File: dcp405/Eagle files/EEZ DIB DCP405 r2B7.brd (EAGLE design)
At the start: 180 x 95 mm, 308 parts, among them IC1 LTC3864EMSE#PBF, IC10 MC33272ADR2G, IC11 LTC2050HVCS8#PBF, IC12 74AUP1G74DC.125, IC13 MCP23S17-E/SS, IC14 REF5025AIDR, IC15 TC77-5.0MCTTR, IC16 DAC8552IDGKR, IC17 SN74LVC1G3157DCKR, IC18 ADS1120IPWR, IC19 LM293D, IC2 TPS54060DGQ, IC20 MAX9141ESA, IC3 SI8641BB-B-IS1, IC4 SN74LVC1G139DCUR, IC5 MC78L05, IC6 MC79L05, IC7 SI8641BB-B-IS1, IC8 M24C32-WMN6P, IC9 MC33272ADR2G, J1 4907, J2 FCR7350R, J3 FCR7350B, K1 G6K-2F-5DC, Q1 SUD19P06-60, Q10 PSMN0R9-25YLC, Q11 PSMN0R9-25YLC, Q12 BSS84P, Q13 BTA26-600, Q14 FMMT493TA, Q15 2N7002, Q16 2N7002, Q17 2N7002, Q18 MMBT5401, Q19 MMBT5551, Q2 MMBT5401, Q20 MMBT5551, Q21 2N7002, Q3 D45H11FP, Q4 D45H11FP, Q5 FQPF11P06 or FQPF27P06, Q6 BCP56-16.115, Q7 MMBT5401, Q8 NZT605, Q9 BSS205NH6327XTSA1, X1 39-30-1020, X2 77317-104-28LF, X3 1844249, X4 DS1024-2*10R0

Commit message: #49
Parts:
- added C97: 10n, rcl:C0805
- added R107: 470R, rcl:R0805
- added R108: 100K, rcl:R0805
- C41: value 1n -> 220p
- C42, C57, C58: value 33p -> 100n; device rcl:C0805 -> rcl:C0603
- C43, C60: value 330p -> 33p
- C44: value 1n -> 330p
- C46: value 10n -> 220p
- C48: value 100n -> 10n; device rcl:C0603 -> rcl:C0805
- C50, C67, C78, C80: value 1u -> 100n; device rcl:C0805 -> rcl:C0603
- C51, C72, C88: value 10n -> 100n; device rcl:C0805 -> rcl:C0603
- C52: value 6n8 -> 1u
- C53: value 1u -> 10n
- C54: value 100n -> 6n8; device rcl:C0603 -> rcl:C0805
- C55, C69, C70, C79, C81: value 100n -> 1u; device rcl:C0603 -> rcl:C0805
- C59: value 4n7 -> 33p
- C61: value 1n -> 4n7
- C62: value 100n -> 330p; device rcl:C0603 -> rcl:C0805
- C63, C86: value 100n -> 1n; device rcl:C0603 -> rcl:C0805
- C64: value 4u7 -> 100n; device rcl:C1206 -> rcl:C0603
- C66: value 4u7 tant. -> 4u7; device EEZ_Lib1:EC1206 -> rcl:C1206
- C68: value 1u -> 4u7 tant.; device rcl:C0805 -> EEZ_Lib1:EC1206
- C73: value 4n7 -> 100n; device rcl:C0805 -> rcl:C0603
- C77: value 100n -> 4n7; device rcl:C0603 -> rcl:C0805
- C82: value N.C. -> 100n; device rcl:C0805 -> rcl:C0603
- C83: value 100n -> N.C.; device rcl:C0603 -> rcl:C0805
- C84: value 1n -> 100n; device rcl:C0805 -> rcl:C0603
- C89: value 470n -> 10n; device rcl:C1206 -> rcl:C0805
- C90: value HHXC630A330MHA0G -> 470n; device EEZ_Lib1:CAPAE830X1050N -> rcl:C1206
- C91: value 10n/200V -> HHXC630A330MHA0G; device rcl:C1206 -> EEZ_Lib1:CAPAE830X1050N
- C92: value N.C. -> 10n/200V; device EEZ_Lib1:ECAP2/5 -> rcl:C1206
- C93: device rcl:C0805 -> EEZ_Lib1:ECAP2/5
- C95: value 10n/200V -> N.C.; device rcl:C1206 -> rcl:C0805
- C96: value 10n -> 10n/200V; device rcl:C0805 -> rcl:C1206
- R100, R46: value 10K -> 2K2
- R101: value 1R -> 10K
- R102: value 750R -> 10K
- R103: value 47K -> 1R
- R104: value 330R -> 750R
- R105: value 470R -> 47K
- R106: value 100K -> 330R
- R50: value 4K7 -> 10K
- R51, R67: value 100K -> 4K7
- R52: value 39K 0.1% -> 100K
- R53: value 820R 0.1% -> 2K2
- R54: value 47K -> 2K2
- R55: value 2K2 -> 39K 0.1%
- R56: value 1R -> 820R 0.1%; device rcl:R1206 -> rcl:R0805
- R57, R62: value 10K -> 47K
- R58: value 1K -> 1R; device rcl:R0805 -> rcl:R1206
- R59: value 39K 0.1% -> 10K
- R60: value 47K -> 1K
- R61: value 0R010 (low TCR) -> 39K 0.1%; device EEZ_Lib1:R_2512-4WIRE -> rcl:R0805
- R63: value 820R 0.1% -> 0R010 (low TCR); device rcl:R0805 -> EEZ_Lib1:R_2512-4WIRE
- R64, R85: value 1K -> 10K
- R65: value 4K7 -> 820R 0.1%
- R66, R99: value 10K -> 1K
- R68: value 270R -> 10K
- R69: value 2K2 -> 100K
- R70: value 470R -> 270R
- R71, R74: value 470R -> 2K2
- R72, R73, R76: value 2K2 -> 470R
- R77: value 10R -> 2K2; device rcl:R1206 -> rcl:R0805
- R78: value 330R -> 2K2
- R79: value 4K7 -> 10R; device rcl:R0805 -> rcl:R1206
- R80: value 470R -> 330R
- R81: value 10K -> 4K7
- R82: value 4K7 -> 470R
- R84: value 330R -> 4K7
- R87: value AC01000002207JA100 -> 1K; device rcl:0411/15 -> rcl:R0805
- R88: value 10K -> 330R
- R89: value 10K -> AC01000002207JA100; device rcl:R0805 -> rcl:0411/15
- R90: value 100K -> 10K
- R91: value 6R2 -> 10K
- R92: value 4K7 -> 100K
- R93: value 10K -> 6R2
- R95: value 330R -> 10K
- R96: value 750R -> 4K7
- R97: value 1K -> 330R
- R98: value 2K2 -> 750R
- moved R74 110.9 mm to (110.7, 24.7), turned to 0 degrees
- moved R72 108.6 mm to (11.8, 69.5), turned to 270 degrees
- moved R68 108.5 mm to (116.2, 63.4)
- moved R84 108.0 mm to (117.7, 53.8), turned to 90 degrees
- moved R76 107.5 mm to (12.4, 76.0), turned to 180 degrees
- moved R73 105.6 mm to (11.8, 65.6), turned to 270 degrees
- moved R96 100.9 mm to (117.7, 49.8), turned to 270 degrees
- moved C88 90.5 mm to (115.7, 45.4), turned to 90 degrees
- moved R95 86.5 mm to (113.9, 56.1)
- moved C72 85.5 mm to (92.3, 30.0)
- moved R89 78.4 mm to (33.3, 61.7)
- moved R69 73.9 mm to (125.5, 65.6), turned to 0 degrees
- moved R82 72.3 mm to (45.5, 49.7), turned to 270 degrees
- moved R88 67.5 mm to (12.4, 79.9), turned to 180 degrees
- moved R93 66.3 mm to (48.4, 45.8)
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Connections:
- new net N$10: C47.1, R53.1, R54.2
- new net N$24: C42.1, R45.1, R46.2
- net !DP_DRIVE: now also R71.1; no longer R69.1
- net !IOEXP_RST: now also C62.1, R66.2; no longer C60.1, R64.2
- net !OVP_FAULT: now also C63.1, R67.2; no longer C61.1, R65.2
- net !SET_DP: now also R69.2; no longer R67.2
- net +5V: now also C63.2, C64.2, C67.1, C79.2, R101.2, R68.1, R69.1, R81.2, R94.2; no longer C60.2, C61.2, C63.1, C77.2, R64.1, R65.1, R79.2, R92.2, R99.2
- net +VREF: now also C68.+, C72.2, C82.2; no longer C66.+, C70.2, C81.2
- net 50MA_S: now also R58.1; no longer R53.1
- net 5A_S: now also R63.2; no longer R61.2
- net AUX_IN: now also R72.1; no longer C72.2, R70.1
- net CC_ACTIVE: now also R94.1, R96.2; no longer R92.1, R94.2
- net CC_LED: now also R88.2; no longer R86.2
- net CURR_50MA: now also R57.2; no longer R54.2
- net CURR_5A: now also R62.2; no longer R60.2
- net CV_ACTIVE: now also R81.1, R84.2; no longer R79.1, R82.2
- net CV_LED: now also R86.1; no longer R84.1
- net D_CC: now also R88.1; no longer R86.1
- net D_CV: now also R86.2; no longer R84.2
- net GCOM: now also R55.1; no longer R52.1
- net GND: now also C42.2, C49.2, C52.1, C56.2, C57.1, C58.1, C64.1, C66.2, C68.-, C69.2, C70.2, C71.1, C73.2, C75.1, C76.2, C82.1, C83.2, C88.1, R105.1, R108.1, R52.1, R57.1, R62.1, R70.2, R76.1, R85.2, R92.1, R93.1; no longer C46.1, C49.1, C54.2, C56.1, C62.1, C63.2, C64.2, C66.-, C68.2, C69.1, C70.1, C71.2, C73.1, C75.2, C76.1, C82.2, C83.1, R103.1, R106.1, R51.1, R54.1, R60.1, R68.2, R74.1, R83.2, R90.1, R91.1
- net ISENSE+: now also R55.2, R56.2; no longer R52.2, R53.2
- net ISENSE-: now also C60.1, R61.1, R65.2; no longer C58.1, R59.1, R63.2
- net I_MON: now also C60.2, R59.1, R61.2, R78.1; no longer C58.2, R57.1, R59.2, R76.1
- net I_SERVO: now also C54.2, C59.2, R95.1; no longer C52.2, C57.2, R93.1
- net I_SET: now also R54.1, R74.1; no longer R55.1, R72.1
- net LOOP_CTRL: now also R91.2; no longer R89.2
- net N$105: now also R84.1; no longer R82.1
- net N$106: now also R96.1; no longer R94.1
- net N$107: now also C89.2, R100.2, R97.1; no longer C88.2, R95.1, R96.2
- net N$108: now also R102.2; no longer R100.2
- net N$109: now also R99.1; no longer R97.1
- net N$11: now also R58.2, R63.2S; no longer R56.2, R61.2S
- net N$110: now also C97.1, R104.1, R106.2; no longer C96.1, R102.1, R104.2
- net N$112: now also R102.1, R105.2; no longer R100.1, R103.2
- net N$113: now also C90.2, R103.2; no longer C89.2, R101.2
- net N$114: now also R107.1; no longer R105.1
- net N$12: now also R70.1; no longer R68.1
- net N$120: now also R107.2; no longer R105.2
- net N$121: now also R76.2; no longer R74.2
- net N$13: now also R87.2; no longer R85.2
- net N$14: now also C44.1; no longer C43.1
- net N$15: now also R89.2; no longer R87.2
- net N$153: now also R83.2; no longer R81.2
- net N$158: now also C43.1; no longer C42.1
- net N$161: now also R95.2; no longer R93.2
- net N$17: now also R72.2, R73.1; no longer R70.2, R71.1
- net N$170: now also R91.1; no longer R89.1
- net N$173: now also R100.1, R99.2; no longer R97.2, R98.1
- net N$18: now also R82.1; no longer R80.1
- net N$19: now also R93.2; no longer R91.2
- net N$200: now also R63.1S, R65.1; no longer R61.1S, R63.1
- net N$21: now also R87.1, R92.2; no longer R85.1, R90.2
- net N$31: now also C86.2, R90.2; no longer C85.2, R88.2
- net N$32: now also R73.2; no longer R71.2
- net N$33: now also C85.2, R80.2, R85.1; no longer C84.2, R78.2, R83.1
- net N$37: now also C54.1, R60.1; no longer C52.1, R58.1
- net N$42: now also R71.2; no longer R69.2
- net N$56: now also R68.2; no longer R66.2
- net N$70: now also C81.2, R79.2; no longer C79.2, R77.2
- net N$71: now also C70.1; no longer C68.1
- net N$72: now also C74.2, R74.2; no longer C73.2, R72.2
- net N$73: now also C77.2, R77.2; no longer C76.2, R75.2
- net N$80: now also C75.2, R75.2; no longer C74.2, R73.2
- net N$81: now also C76.1, R78.2; no longer C75.1, R76.2
- net N$82: now also R53.2; no longer R55.2
- net N$84: now also R51.2; no longer R46.2
- net N$88: now also C61.2, R64.1; no longer C59.2, R62.1
- net N$89: now also C59.1, R59.2, R60.2, R64.2; no longer C57.1, R57.2, R58.2, R62.2
- net N$91: now also C46.2, R51.1; no longer C44.2, R50.1
- net OUTC+: now also C92.1, C93.+, C95.1; no longer C91.1, C92.+, C93.1
- net OUTC-: now also C93.-, C96.2; no longer C92.-, C93.2
- net OUTF+: now also R82.2; no longer R80.2
- net PE: now also C92.2, C96.1; no longer C91.2, C95.1
- net POST_OE: now also R52.2; no longer R51.2
- net POST_OUT+: now also C46.1, C61.1; no longer C44.1, C59.1
- net POST_OUT-: now also C91.-, C97.2, R103.1, R106.1; no longer C90.-, C96.2, R101.1, R104.1
- net POST_OUTF+: now also C90.1, C91.+, R97.2; no longer C88.1, C90.+, R95.2
- net PREG_OUT-: now also R63.1, R89.1; no longer R61.1, R87.1
- net RSENSE: now also R108.2; no longer R106.2
- net SENSE+: now also R98.1; no longer R96.1
- net SENSE-: now also R104.2; no longer R102.2
- net SENSE_ERR: now also R101.1; no longer R99.1
- net U_MON: now also C43.2, R50.1, R77.1, R80.1; no longer C42.2, R46.1, R75.1, R78.1
- net U_SERVO: now also C44.2, R83.1; no longer C43.2, R81.1
- net U_SET: now also R75.1, R90.1; no longer R73.1, R88.1
- net U_SET_OUT: now also R46.1; no longer R45.1
- net V+: now also C49.1, C51.2, C52.2, C66.1, C69.1, C71.2, C73.1, C83.1, C84.2, C87.2, R79.1; no longer C46.2, C47.1, C49.2, C64.1, C67.1, C69.2, C71.1, C82.1, C83.2, C86.2, R77.1
- net V-: now also C56.1, C57.2, C58.2, C88.2; no longer C51.2, C54.1, C56.2, C87.2
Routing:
- net U_SET: track 67.1 -> 61.6 mm, vias 2 -> 4
- net N$10: track 0.00 -> 3.78 mm
- net N$24: track 0.00 -> 3.69 mm
- net AUX_IN: track 104.5 -> 101.4 mm
- net GND: track 195.9 -> 198.4 mm
- net I_SET: track 28.4 -> 26.2 mm
- net U_SET_OUT: track 7.11 -> 5.30 mm, vias 2 -> 0
- net AUX_USET_SW: track 168.9 -> 167.2 mm
- net POST_OUT-: track 234.3 -> 233.3 mm
- net SENSE-: track 74.1 -> 73.0 mm
- net SENSE+: track 75.5 -> 74.5 mm
- net +VREF: track 59.2 -> 60.3 mm
- net U_MON: track 75.9 -> 76.6 mm
- net V-: track 129.9 -> 130.4 mm
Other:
- board text added: "B"
- board text added: "EEZ DIB DCP405 (10/2019 r2B7)"
- board text added: "EEZ DIB DCP405 (10/2019 r2B7) DC power source 0-40V / 5A Project source code: github.com/eez-open"
- board text removed: "EEZ DIB DCP405 (09/2019 r2B6)"
- board text removed: "EEZ DIB DCP405 (09/2019 r2B6) DC power source 0-40V / 5A Project source code: github.com/eez-open"

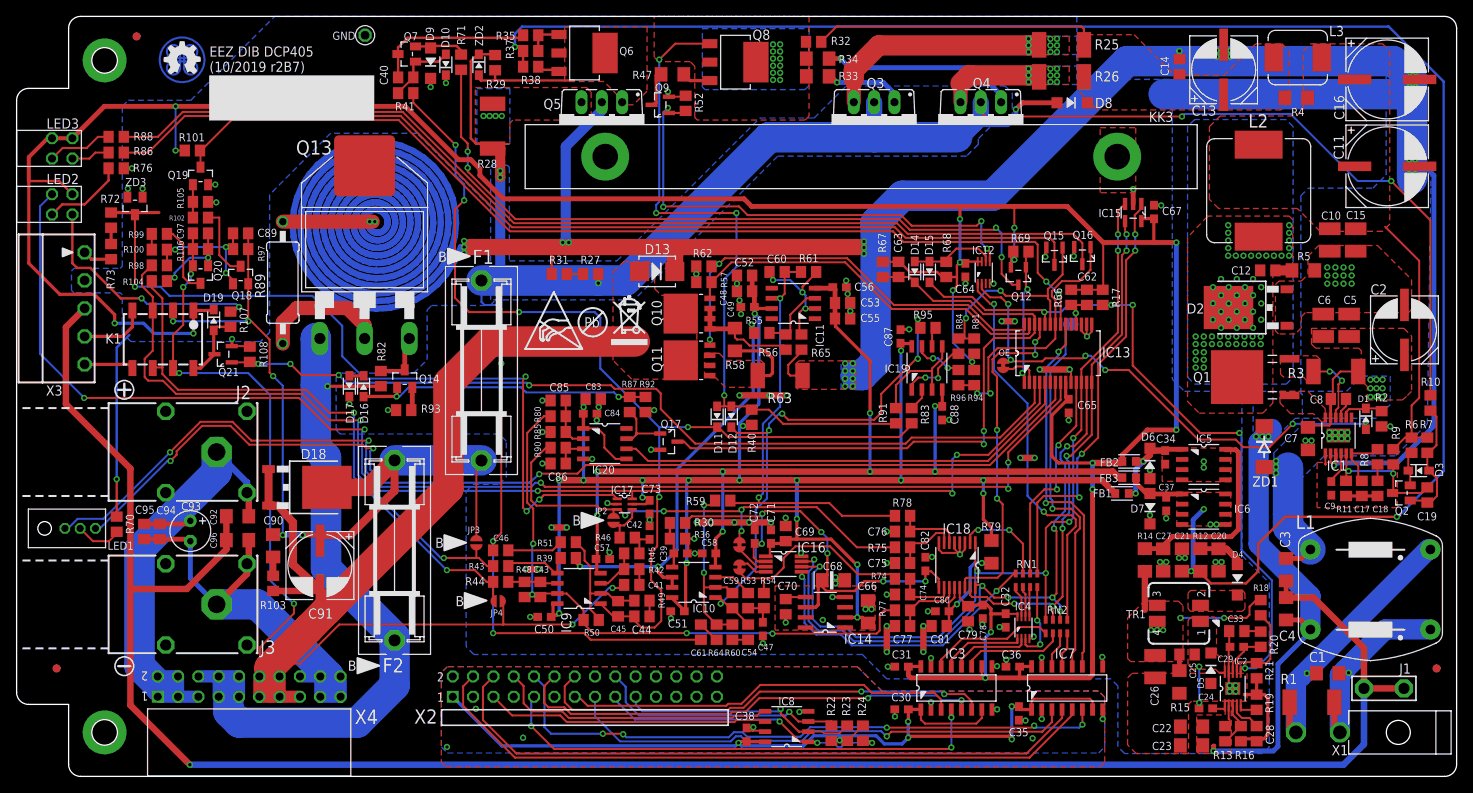
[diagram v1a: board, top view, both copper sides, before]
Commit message: DCP405 OVP up-programming adjustment
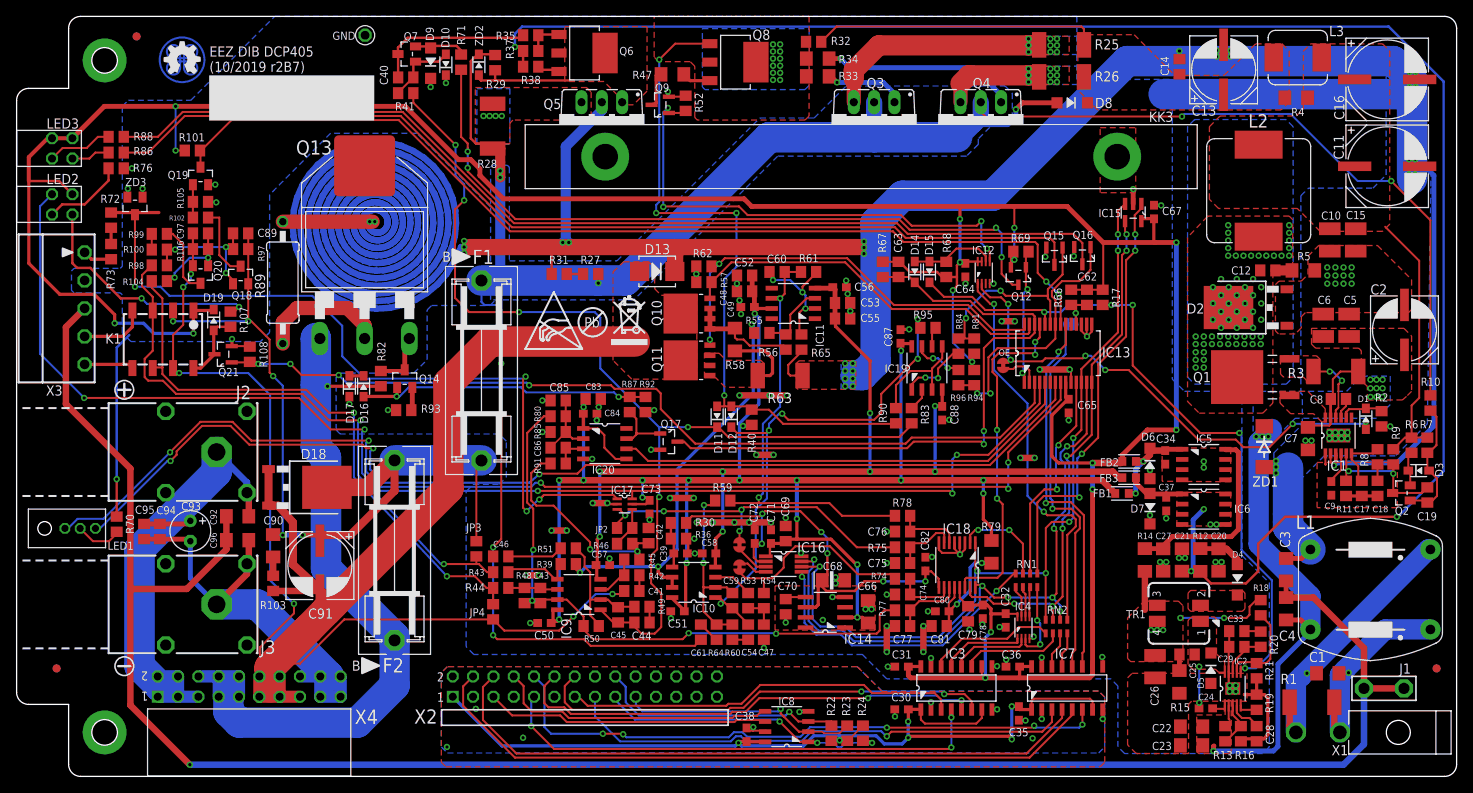
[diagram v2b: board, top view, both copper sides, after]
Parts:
- C29: device rcl:C0603 -> rcl:C0805
- C42, C47: value 100n -> 470n; device rcl:C0603 -> rcl:C0805
- C86: value 1n -> 33n
- JP2, JP3, JP4: value JP2-CUT -> JP2-CUT-0805; device EEZ_Lib1:JP2-CUT -> EEZ_Lib1:R_0805
- R89: value AC01000002207JA100 -> AC01000001007JA100
- moved R91 42.6 mm to (67.7, 39.1), turned to 0 degrees
- moved R90 42.4 mm to (109.9, 45.1), turned to 270 degrees
- moved C86 1.97 mm to (67.7, 41.1)
- moved JP2 1.69 mm to (76.0, 31.1), turned to 0 degrees
- moved JP4 1.48 mm to (59.6, 20.6), turned to 90 degrees
- moved R46 0.83 mm to (76.0, 29.1)
- moved C41 0.76 mm to (76.9, 23.2)
- moved C44 0.76 mm to (78.2, 19.2)
- moved C46 0.76 mm to (60.5, 27.5)
- moved C50 0.76 mm to (66.0, 19.2)
- moved C57 0.76 mm to (73.3, 26.4)
- moved IC9 0.76 mm to (70.3, 22.7)
- moved JP3 0.76 mm to (57.5, 28.4)
- moved R39 0.76 mm to (69.0, 26.5)
- moved R42 0.76 mm to (76.9, 25.1)
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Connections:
- removed net N$24: C42.1, R45.1, R46.2
- new net U_SET_OVP: C42.1, R45.1, R46.2, R91.1
- net GND: no longer C86.1
- net LOOP_CTRL: now also R90.2; no longer R91.2
- net N$170: now also R90.1; no longer R91.1
- net N$31: now also R91.2; no longer R90.2
- net N$33: now also C86.1
- net U_SET: no longer R90.1
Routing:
- net U_SET_OVP: track 0.00 -> 27.5 mm, vias 0 -> 2
- net U_SET: track 61.6 -> 43.4 mm
- net GND: track 198.4 -> 204.9 mm, vias 112 -> 116
- net N$24: track 3.69 -> 0.00 mm
- net N$33: track 6.47 -> 9.23 mm
- net POST_OUT-: track 233.3 -> 231.2 mm
- net U_MON: track 76.6 -> 77.7 mm
- net POST_OUT+: track 285.7 -> 286.5 mm
- net V+: track 227.5 -> 228.3 mm
- net U_SERVO: track 132.2 -> 133.0 mm
- net V-: track 130.4 -> 130.9 mm
- net SENSE-: track 73.0 -> 73.6 mm

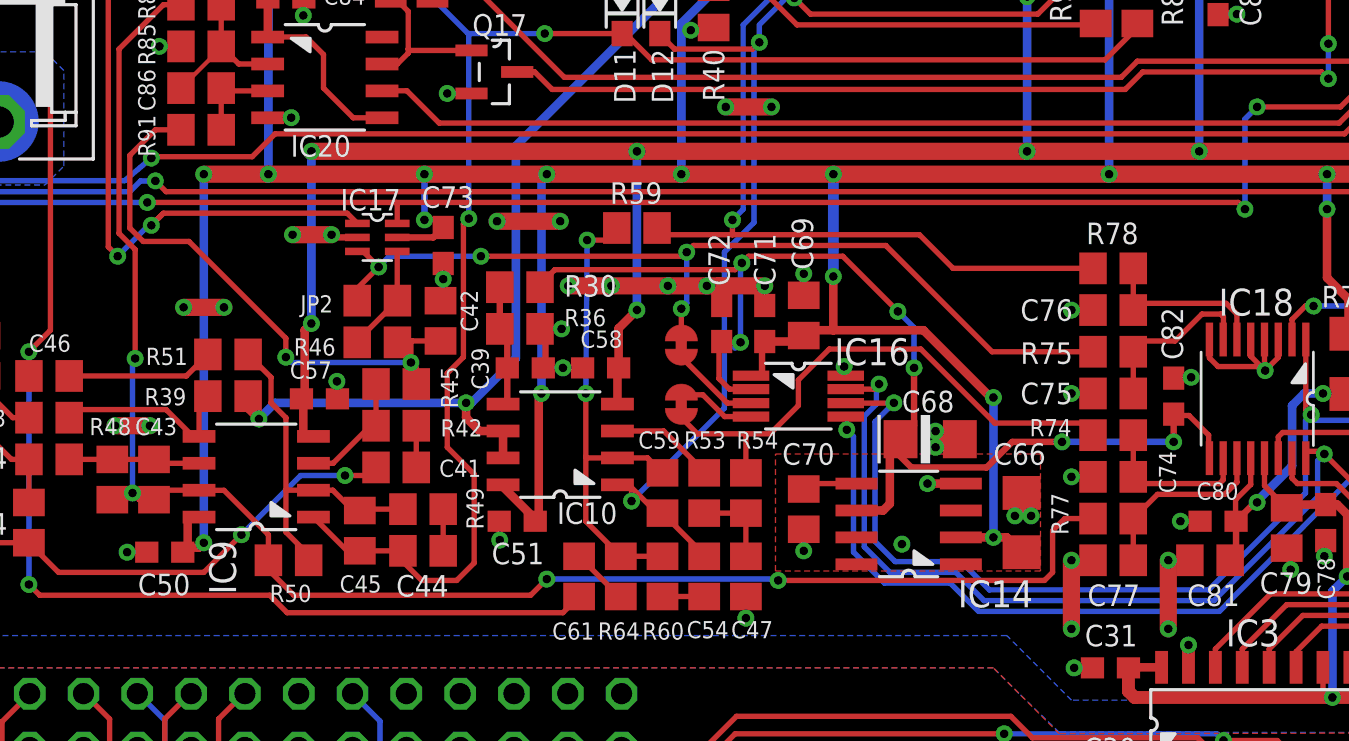
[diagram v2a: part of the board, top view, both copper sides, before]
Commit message: DCP405 OVP U_SET fixed
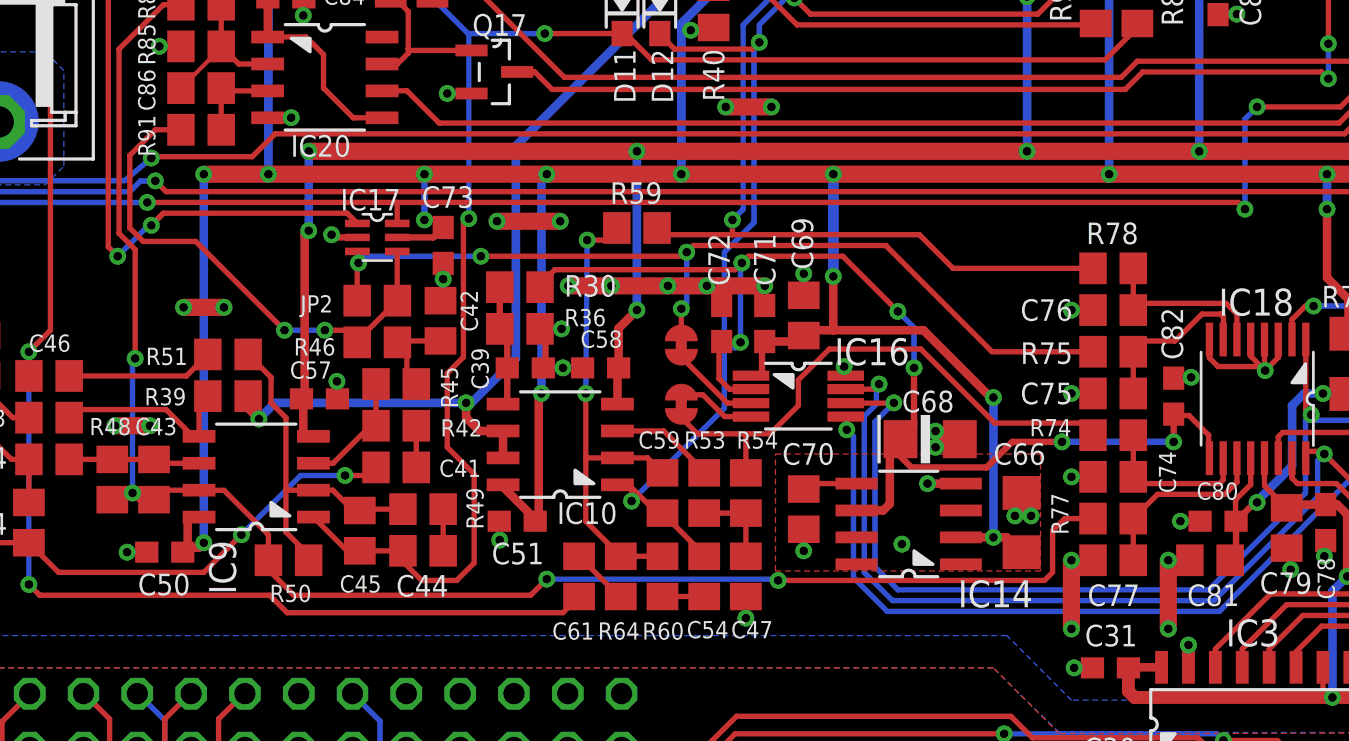
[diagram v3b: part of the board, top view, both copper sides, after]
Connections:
- net U_SET_OUT: now also R91.1
- net U_SET_OVP: no longer R91.1
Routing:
- net U_SET_OVP: track 27.5 -> 4.62 mm, vias 2 -> 0
- net U_SET_OUT: track 5.08 -> 24.4 mm, vias 0 -> 2
- net GND: track 204.9 -> 203.1 mm, vias 116 -> 115
- net MOSI: track 80.1 -> 80.8 mm
- net CS_DAC: track 37.8 -> 38.5 mm
- net SCLK: track 105.9 -> 106.6 mm
